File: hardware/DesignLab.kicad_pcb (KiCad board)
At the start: 2 copper layers, 169.9 x 180.3 mm, 83 parts, among them J1 Micro_SD_Card_Det, J2 Conn_01x04_Female, P1 USB_C_Plug_USB2.0, Q1 DMG3415U-7, SW1 SW_DPDT_x2, SW10 Button, SW11 Button, SW12 RESET, SW13 ON, SW14 VOL, SW15 BOOT, SW3 REC, SW4 Button, SW5 Button, SW6 Button, SW7 Button, SW8 Button, SW9 Button, U1 SPH0641LM4H, U10 MCP4018-xxxxLT, U2 RP2040, U3 QRE1113, U4 QRE1113, U5 QRE1113, U6 W25Q80DVSSIG, U7 PAM8302AASCR, U8 AP2112K-3.3, U9 QRE1113, Y1 12Mhz, sw2 SW_DPDT_x2

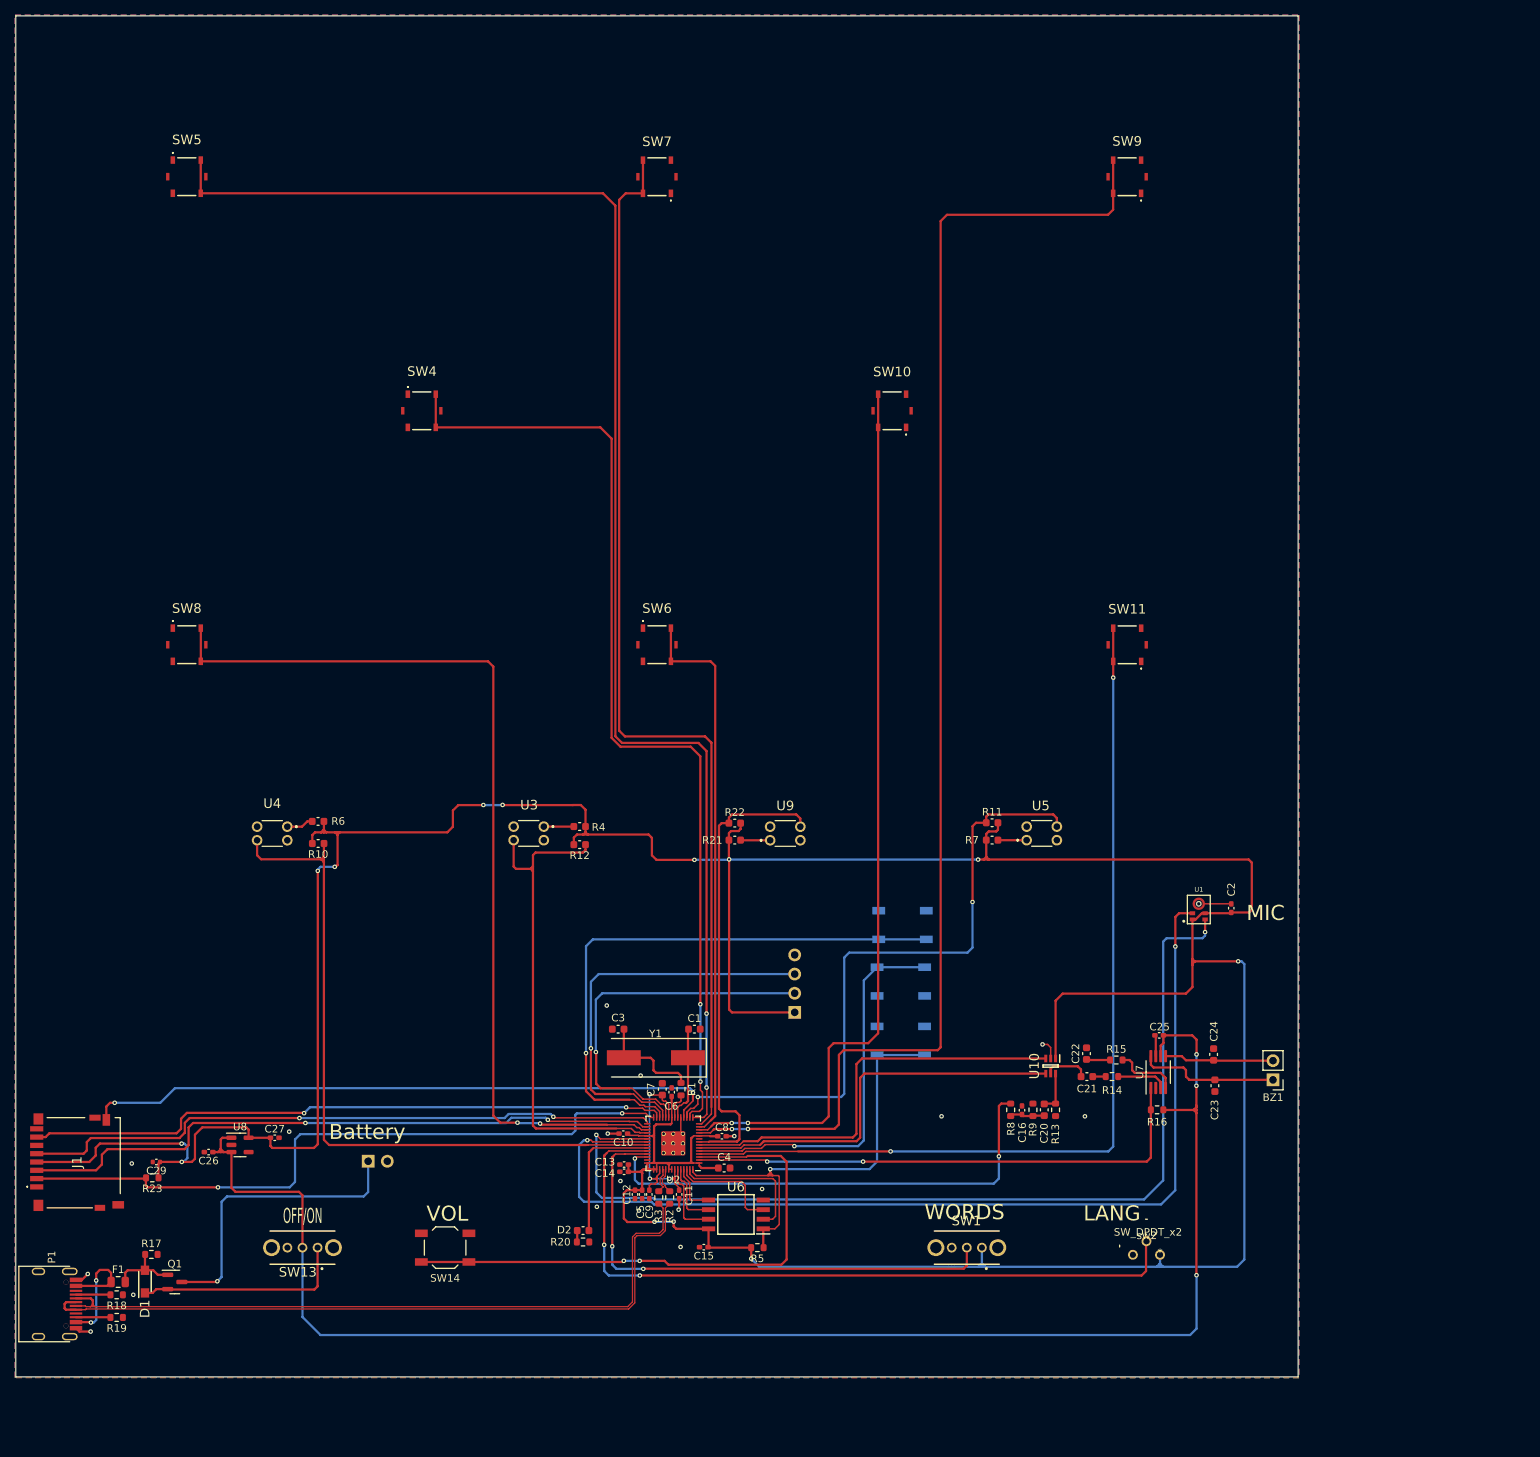
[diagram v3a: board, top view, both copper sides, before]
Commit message: Buttons were changed, routed and assigned another pin
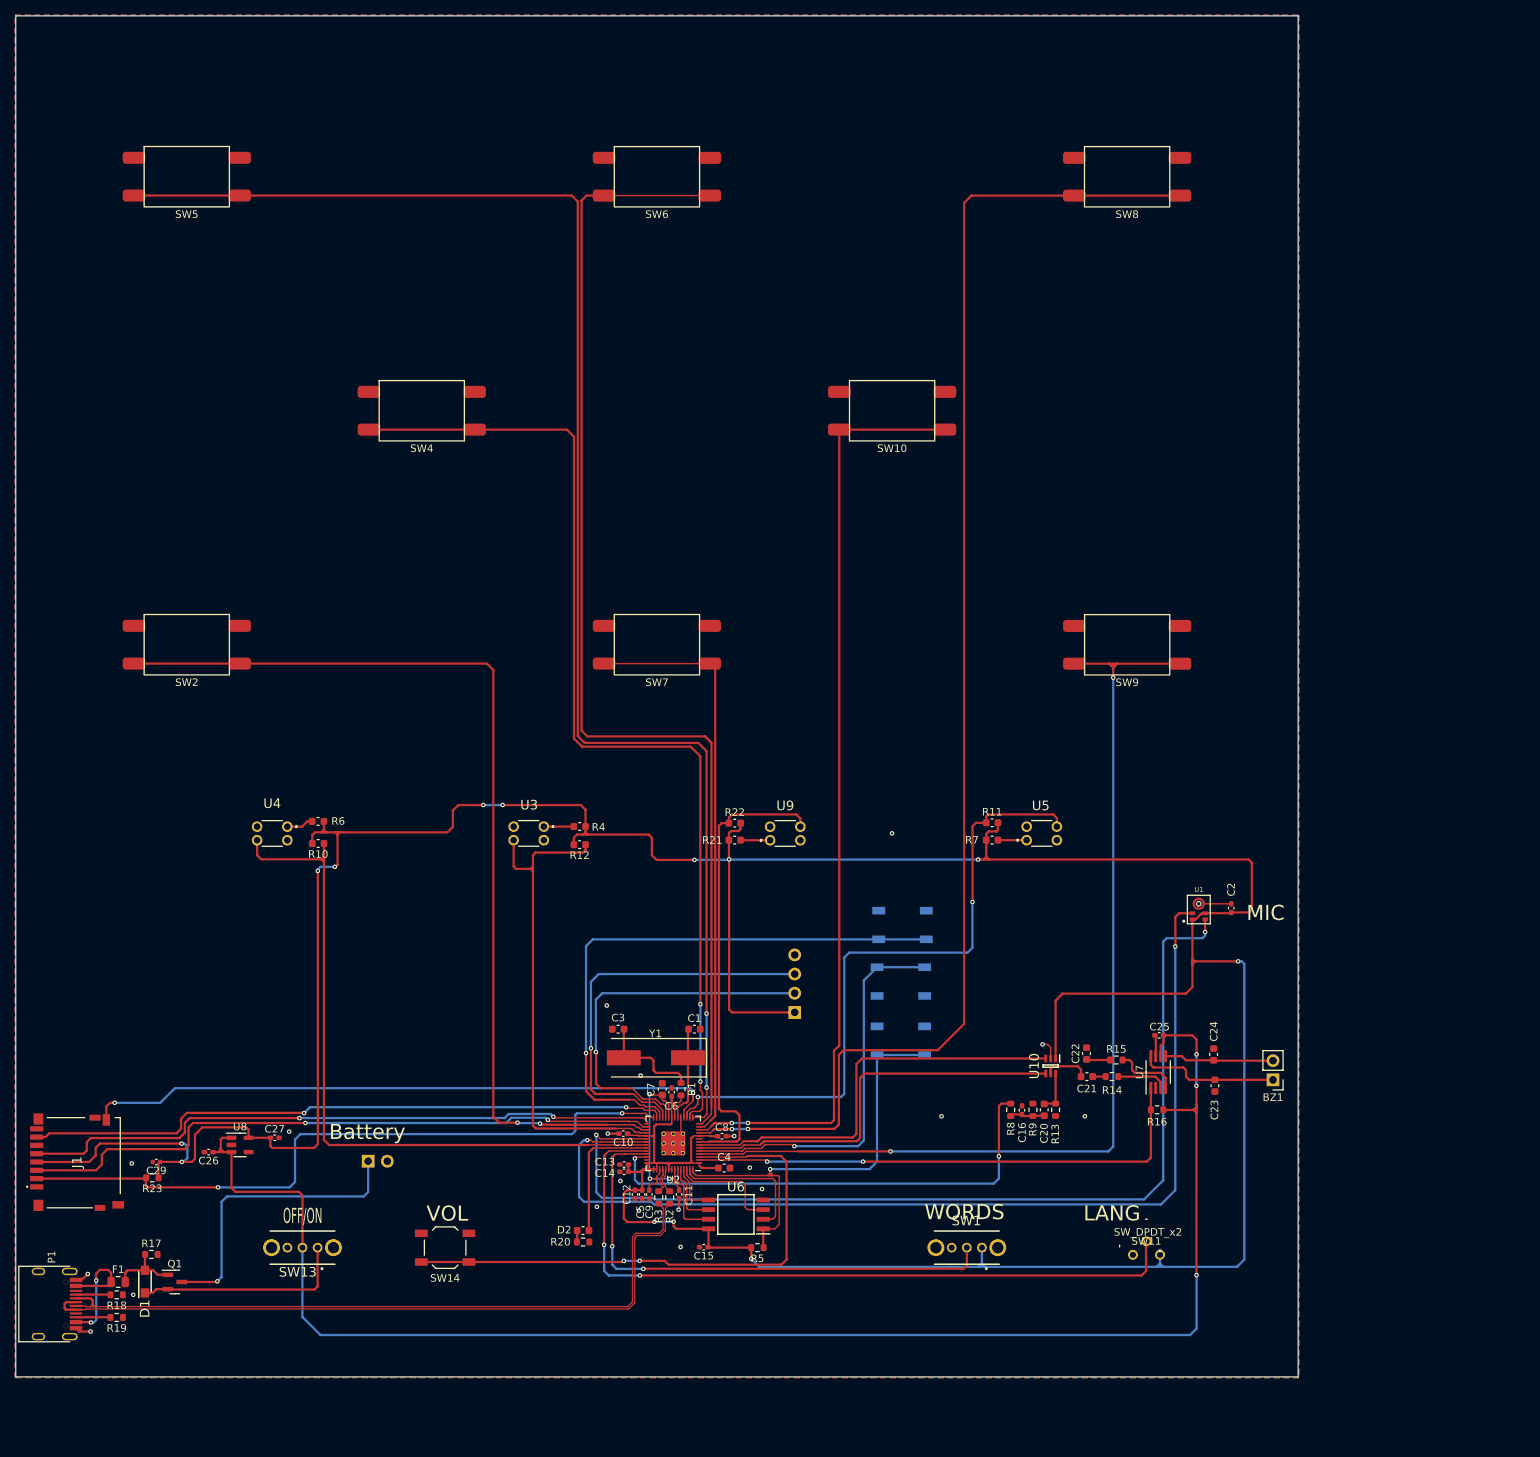
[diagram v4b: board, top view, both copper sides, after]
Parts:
- removed sw2: SW_DPDT_x2, Design:7829H-1-051LF
- added SW2: SW_Push, Design:Button, F.Cu at (141.8, 114.1)
- SW10, SW4, SW5, SW6, SW7, SW8, SW9: value Button -> SW_Push; footprint Design:EVQPLFA08 -> Design:Button
- SW11: value Button -> SW_DPDT_x2; footprint Design:EVQPLFA08 -> Design:7829H-1-051LF
- moved SW8 139.2 mm to (266.4, 52.0)
- moved SW11 80.9 mm to (270.8, 194.9)
- moved SW9 62.0 mm to (266.4, 114.1), turned to 0 degrees
- moved SW6 62.0 mm to (204.1, 52.0)
- moved SW7 62.0 mm to (204.1, 114.1), turned to 0 degrees
- turned SW10 to 0 degrees
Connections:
- U2 pad 11: /D5 -> /D2
- U2 pad 12: /D6 -> /D4
- U2 pad 13: /D0 -> /D6
- U2 pad 15: /D2 -> /D0
- U2 pad 31: /D7 -> /D5
- U2 pad 4: /D4 -> /D7
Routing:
- net /D0: track 72.9 -> 198.0 mm, vias 0 -> 2
- net /D5: track 181.6 -> 128.3 mm
- net /D6: track 119.0 -> 77.2 mm, vias 2 -> 0
- net /D1: track 142.5 -> 156.7 mm
- net /D7: track 124.2 -> 135.3 mm
- net /D2: track 193.4 -> 184.3 mm
- net /D3: track 130.0 -> 134.5 mm
- net GND: vias 19 -> 20

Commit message: Rounded PCB and added new labels
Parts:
- moved C20 31.1 mm to (285.3, 184.1)
- moved R9 31.1 mm to (283.8, 184.1)
- moved SW3 31.1 mm to (266.3, 167.1)
- moved P1 31.1 mm to (156.2, 209.9)
- moved C24 31.1 mm to (307.8, 176.8)
- moved C25 31.1 mm to (300.6, 174.3)
- moved C26 31.1 mm to (174.6, 189.7)
- moved C27 31.1 mm to (183.4, 187.8)
- moved C29 31.1 mm to (167.7, 191.1)
- moved C6 31.1 mm to (236.0, 181.8)
- moved D1 31.1 mm to (166.2, 206.9)
- moved D2 31.1 mm to (224.2, 200.1)
- moved R1 31.1 mm to (237.2, 181.4)
- moved R13 31.1 mm to (286.8, 184.1)
- moved R15 31.1 mm to (294.9, 177.5)
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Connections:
- R10 pad 1: /S2 -> /S4
- R22 pad 1: /S4 -> /S2
- U2 pad 36: /S2 -> /S4
- U2 pad 8: /S4 -> /S2
- U4 pad 3: /S2 -> /S4
- U9 pad 3: /S4 -> /S2
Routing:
- net /S4: track 62.3 -> 94.5 mm
- net /S2: track 94.5 -> 62.3 mm
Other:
- outline, holes or cut-outs redrawn
- board text added: "+"
- board text added: "-"
- board text added: "LANG 1/LANG 2"
- board text added: "WORDS/PHRASES"
- board text removed: "LANG"
- board text removed: "WORDS"

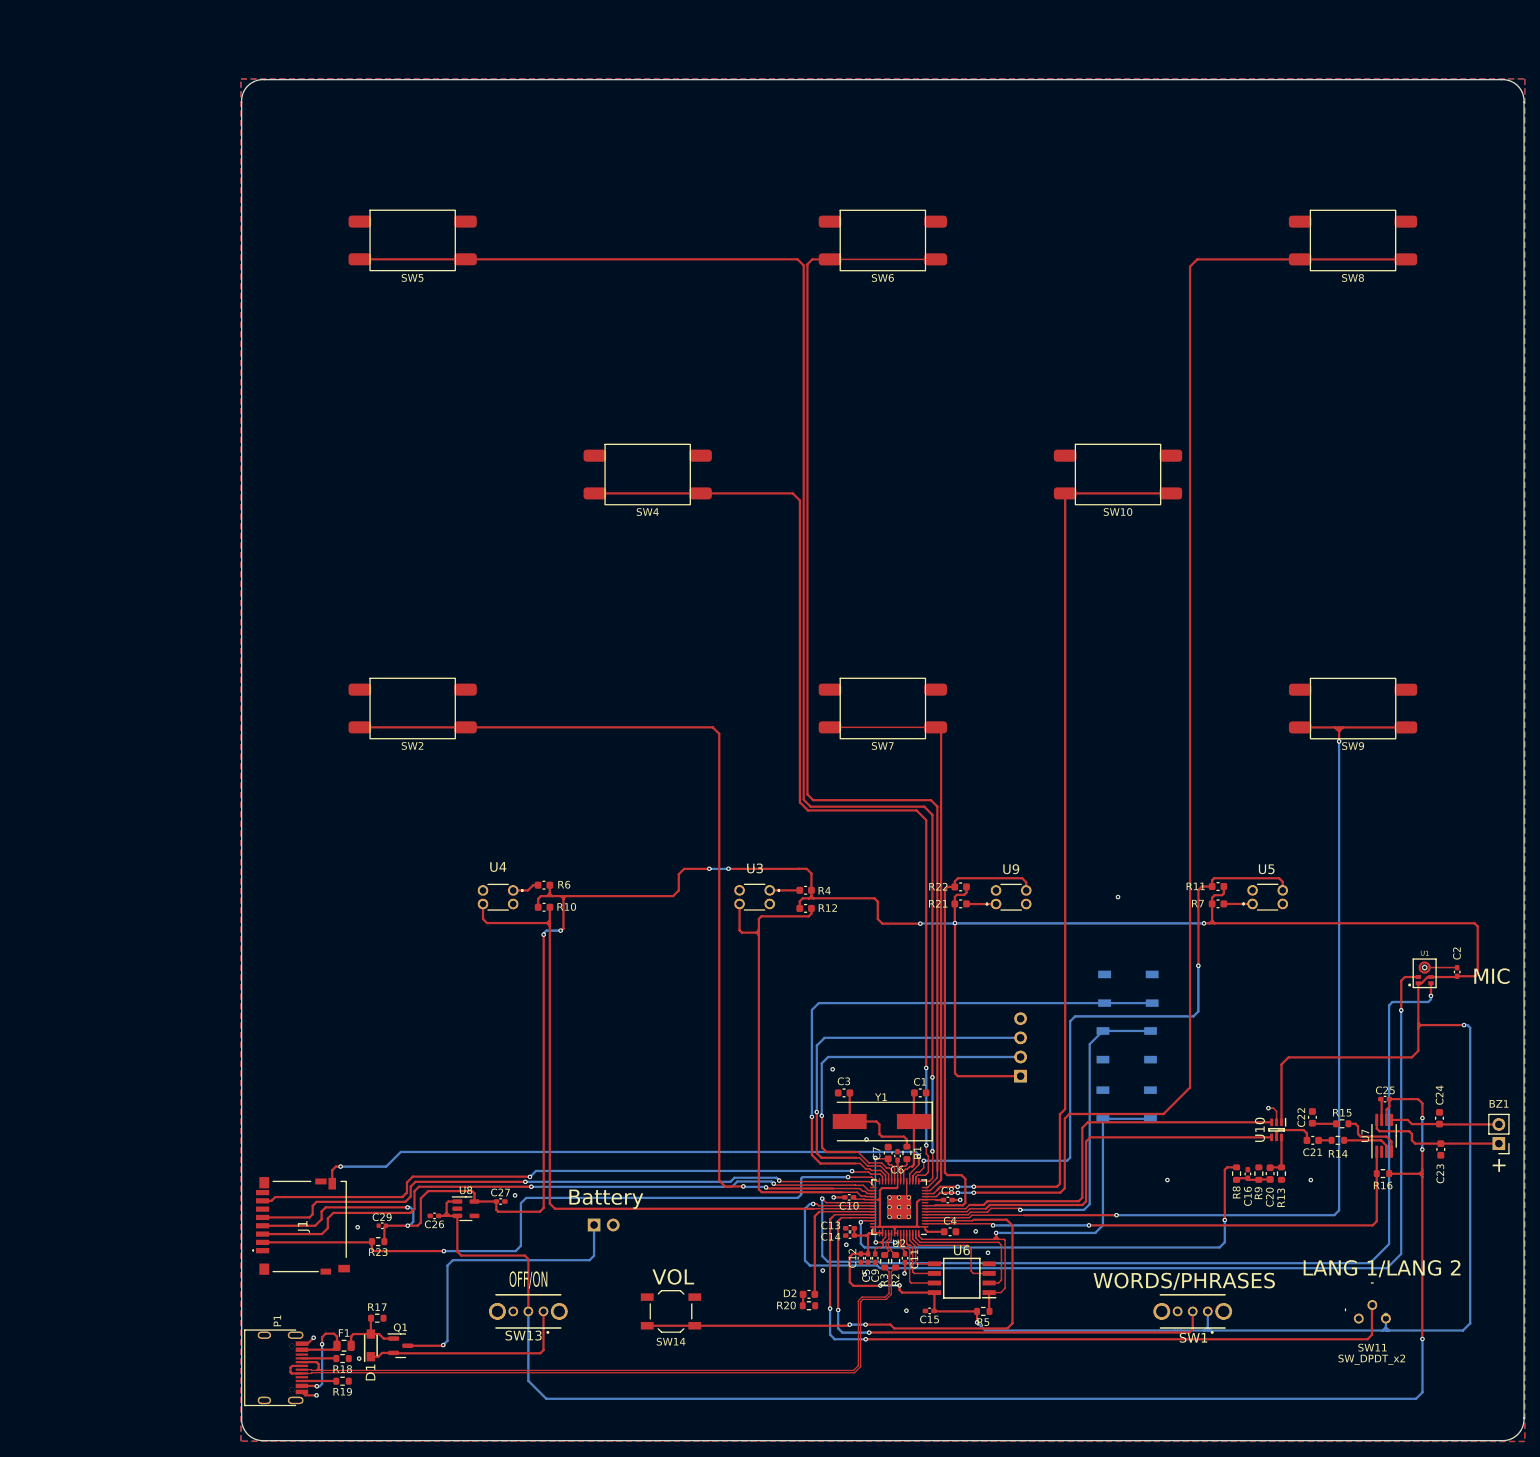
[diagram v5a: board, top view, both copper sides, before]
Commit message: PCB modified and generated another design with the button
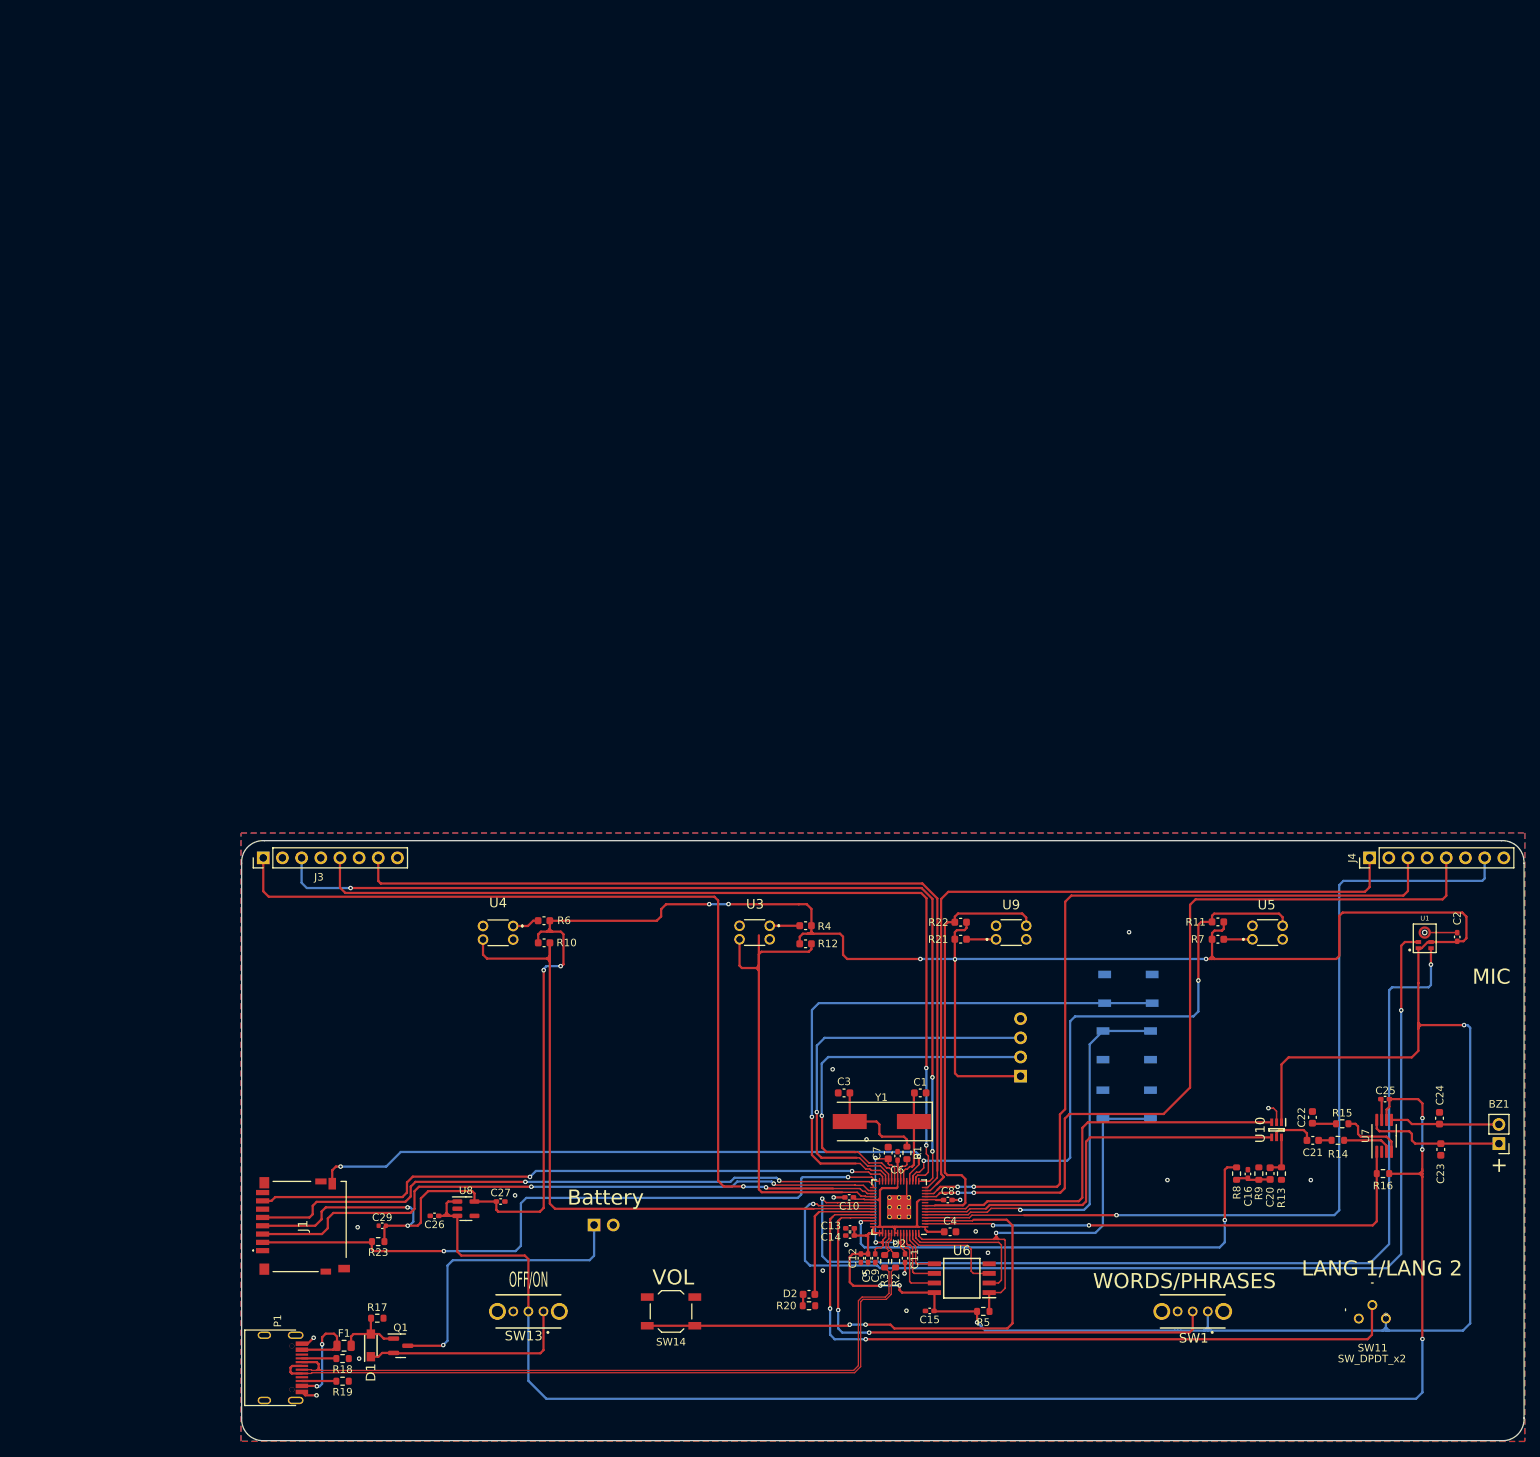
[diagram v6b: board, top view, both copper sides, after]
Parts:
- removed SW10, SW2, SW4, SW5, SW6, SW7, SW8, SW9: SW_Push, Design:Button
- added J3: Conn_01x08, Connector_PinHeader_2.54mm:PinHeader_1x08_P2.54mm_Vertical, F.Cu at (151.9, 142.3)
- added J4: Conn_01x08, Connector_PinHeader_2.54mm:PinHeader_1x08_P2.54mm_Vertical, F.Cu at (298.5, 142.3)
- moved R10 4.71 mm to (189.1, 153.6)
- moved R6 4.71 mm to (189.1, 150.6)
- moved U4 4.71 mm to (185.0, 151.3)
- moved R11 4.69 mm to (278.4, 150.8)
- moved R7 4.69 mm to (278.4, 153.1)
- moved U5 4.69 mm to (283.0, 153.1)
- moved R12 4.69 mm to (223.8, 153.7)
- moved R4 4.69 mm to (223.8, 151.3)
- moved U3 4.69 mm to (219.0, 151.3)
- moved R21 4.68 mm to (244.3, 153.1)
- moved R22 4.68 mm to (244.3, 150.8)
- moved U9 4.68 mm to (249.0, 153.1)
- moved U1 4.64 mm to (305.8, 152.2)
- moved C2 4.64 mm to (310.1, 152.8)
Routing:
- net /D2: track 184.3 -> 110.2 mm
- net /D0: track 198.0 -> 126.8 mm, vias 2 -> 3
- net /D1: track 156.7 -> 117.3 mm
- net /D6: track 77.2 -> 101.5 mm
- net /D4: track 124.2 -> 106.5 mm
- net /D7: track 135.3 -> 120.7 mm, vias 2 -> 1
- net /D3: track 134.5 -> 121.1 mm
- net +3V3: track 524.7 -> 519.5 mm
- net /S1: track 89.2 -> 84.4 mm
- net /DOUT: track 130.8 -> 135.5 mm
- net /S2: track 62.3 -> 57.7 mm
- net /D5: track 128.3 -> 123.6 mm
- net /CLK: track 135.1 -> 139.8 mm
- net /S4: track 94.5 -> 92.3 mm
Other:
- board size 169.9 x 180.3 mm -> 169.9 x 79.5 mm
